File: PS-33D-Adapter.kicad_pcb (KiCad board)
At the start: 2 copper layers, 15 x 7.6 mm, 8 parts, among them J1 CONN_05, J2 Conn_02x04_Counter_Clockwise, Q1 MOSFET-NCH-BSS138, Q2 MOSFET-NCH-BSS138

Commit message: feat: update footprints of connectors
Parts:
- J1: footprint Connector_PinHeader_1.27mm:PinHeader_1x05_P1.27mm_Vertical -> Connector_PinHeader_2.54mm:PinHeader_1x05_P2.54mm_Vertical
- J2: footprint Connector_PinHeader_1.27mm:PinHeader_2x04_P1.27mm_Vertical -> Connector_PinSocket_2.54mm:PinSocket_2x04_P2.54mm_Vertical
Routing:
- net SDA: track 9.40 -> 10.7 mm
- net SCL: track 14.4 -> 13.2 mm

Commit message: feat: remove all traces
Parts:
- moved J2 3.45 mm to (160.3, 77.5)
- moved J1 2.55 mm to (147.1, 76.2)
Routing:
- net 3V3: track 21.2 -> 0.00 mm, vias 1 -> 0
- net SCL: track 13.2 -> 0.00 mm, vias 1 -> 0
- net SDA: track 10.7 -> 0.00 mm, vias 1 -> 0
- net M.SCL: track 10.6 -> 0.00 mm, vias 3 -> 0
- net M.SDA: track 8.42 -> 0.00 mm, vias 2 -> 0
- net 5V: track 5.65 -> 0.00 mm
- removed copper zone on B.Cu, net GND
- removed copper zone on F.Cu, net GND
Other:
- board outline removed

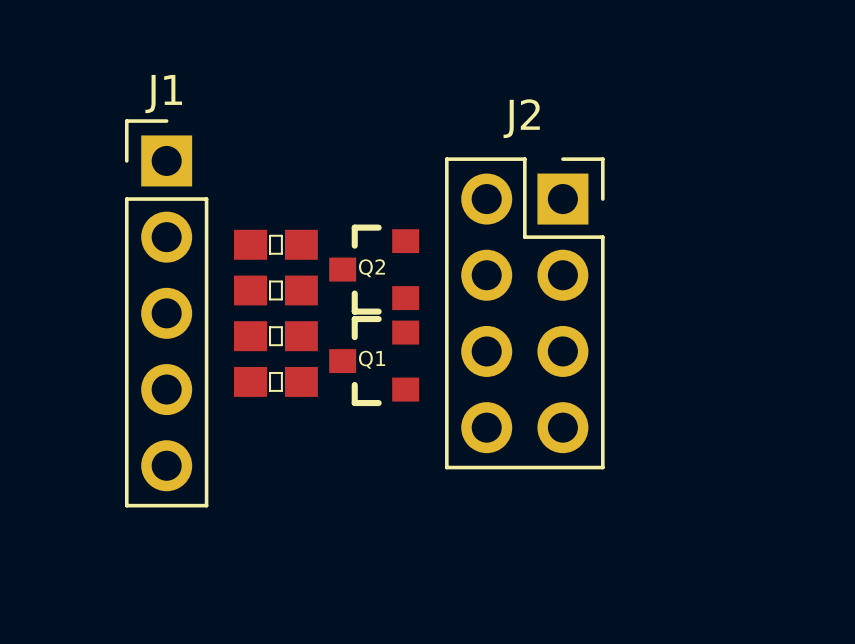
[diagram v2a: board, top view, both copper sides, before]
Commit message: feat: add edge cut
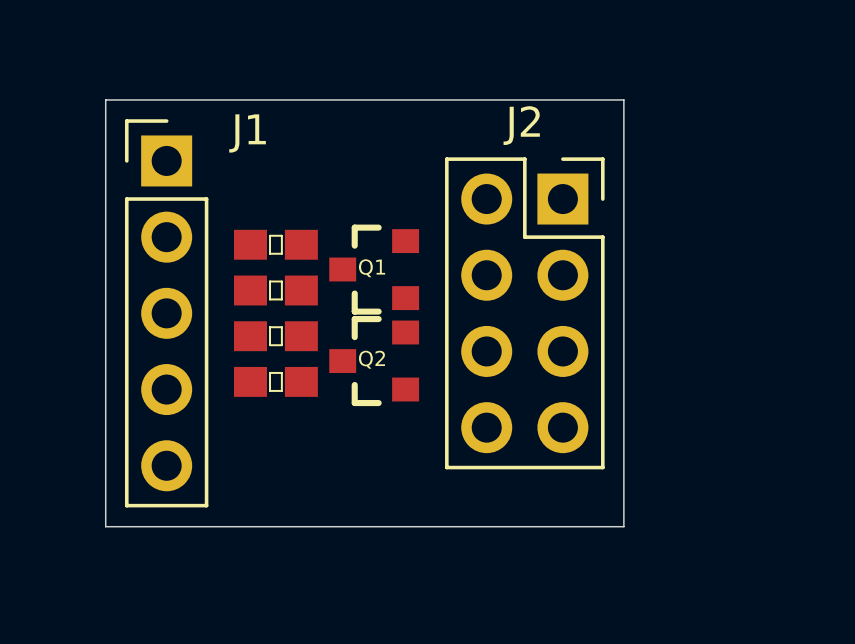
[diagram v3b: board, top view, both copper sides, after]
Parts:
- moved Q1 3.05 mm to (154.0, 79.8)
- moved Q2 3.05 mm to (154.0, 82.9)
- moved R1 3.05 mm to (150.7, 83.6)
- moved R2 3.05 mm to (150.7, 80.5)
- moved R3 3.05 mm to (150.7, 82.0)
- moved R4 3.05 mm to (150.7, 79.0)
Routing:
- net 5V: track 0.00 -> 0.51 mm
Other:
- board outline added: 17.3 x 14.2 mm

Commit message: feat: update pcb
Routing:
- net 3V3: track 0.00 -> 26.1 mm
- net M.SCL: track 0.00 -> 17.6 mm, vias 0 -> 2
- net SDA: track 0.00 -> 16.7 mm, vias 0 -> 2
- net M.SDA: track 0.00 -> 16.6 mm
- net SCL: track 0.00 -> 9.51 mm, vias 0 -> 1
- net 5V: track 0.51 -> 4.93 mm

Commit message: feat: update pcb
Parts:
- moved Q1 4.52 mm to (150.9, 83.1)
- moved Q2 4.43 mm to (150.9, 79.8)
- moved R3 3.54 mm to (153.4, 79.8), turned to 90 degrees
- moved R2 3.48 mm to (148.3, 83.1), turned to 270 degrees
- moved R1 2.75 mm to (153.4, 83.1), turned to 90 degrees
- moved R4 2.49 mm to (148.3, 79.8), turned to 270 degrees
- moved J2 1.80 mm to (158.5, 77.7)
- moved J1 1.27 mm to (145.8, 76.2)
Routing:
- net M.SCL: track 17.6 -> 6.85 mm, vias 2 -> 0
- net M.SDA: track 16.6 -> 6.24 mm
- net 5V: track 4.93 -> 10.5 mm, vias 0 -> 1
- net SDA: track 16.7 -> 12.5 mm
- net 3V3: track 26.1 -> 23.8 mm, vias 0 -> 2
- net SCL: track 9.51 -> 10.3 mm
- added copper zone on B.Cu, net GND
- added copper zone on F.Cu, net GND
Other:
- board size 17.3 x 14.2 mm -> 16.8 x 14.2 mm

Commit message: feat: update schematic, pcb
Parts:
- removed the J2 at (158.5, 77.7)
- added J1: CONN_04, Connector_PinHeader_2.54mm:PinHeader_1x04_P2.54mm_Vertical, F.Cu at (157.5, 77.7)
- added J3: CONN_04, Connector_PinHeader_2.54mm:PinHeader_1x04_P2.54mm_Vertical, F.Cu at (162.6, 77.7)
- renumbered J1 to J2
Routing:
- net 3V3: track 23.8 -> 0.00 mm, vias 2 -> 0
- net SDA: track 12.5 -> 0.00 mm, vias 2 -> 0
- net 5V: track 10.5 -> 0.00 mm, vias 1 -> 0
- net SCL: track 10.3 -> 0.00 mm, vias 1 -> 0
- net M.SCL: track 6.85 -> 0.00 mm
- net M.SDA: track 6.24 -> 0.00 mm
- removed copper zone on B.Cu, net GND
- removed copper zone on F.Cu, net GND
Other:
- board size 16.8 x 14.2 mm -> 20.8 x 14.2 mm

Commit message: feat: update pcb
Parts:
- moved J1 4.10 mm to (161.5, 77.2)
- moved J3 4.10 mm to (166.6, 77.2)
- moved Q1 3.06 mm to (153.9, 82.8)
- moved Q2 3.06 mm to (153.9, 79.5)
- moved R1 3.06 mm to (156.5, 82.8)
- moved R3 3.06 mm to (156.5, 79.5)
- moved R2 3.06 mm to (151.4, 82.8)
- moved R4 3.06 mm to (151.4, 79.5)
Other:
- board outline removed
- board text added: "3V3"
- board text added: "5V"
- board text added: "GND"
- board text added: "SCL"
- board text added: "SDA"

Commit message: feat: update pcb
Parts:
- moved J1 1.52 mm to (160.0, 77.2)
- moved J3 1.52 mm to (165.1, 77.2)
- moved Q1 0.76 mm to (154.7, 82.8)
- moved Q2 0.76 mm to (154.7, 79.5)
- moved R1 0.76 mm to (157.2, 82.8)
- moved R2 0.76 mm to (152.1, 82.8)
- moved R3 0.76 mm to (157.2, 79.5)
- moved R4 0.76 mm to (152.1, 79.5)
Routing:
- net 3V3: track 0.00 -> 32.5 mm
- net 5V: track 0.00 -> 11.6 mm
- net SCL: track 0.00 -> 9.91 mm
- net SDA: track 0.00 -> 9.60 mm
- net M.SCL: track 0.00 -> 9.58 mm, vias 0 -> 1
- net M.SDA: track 0.00 -> 9.26 mm, vias 0 -> 1
- added copper zone on B.Cu, net GND
- added copper zone on F.Cu, net GND
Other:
- board outline added: 23.4 x 14.2 mm
